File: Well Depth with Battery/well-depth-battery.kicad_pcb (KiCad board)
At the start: 2 copper layers, 28 x 26 mm, 59 parts, among them J1 Conn_01x02_Female, J2 Conn_01x04_Female, J3 Conn_01x04_Male, J4 Conn_01x02_Male, J5 USB_A, Q1 Q_NMOS_GSD, Q2 Q_PMOS_GSD, Q3 Q_PMOS_GSD, U1 LM358, U2 LM358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

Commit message: WDB: Floorplanning
Also fixed .gitignore to not ignore lib
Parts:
- removed H4: MountingHole, MountingHole:MountingHole_3.2mm_M3
- J5: footprint Connector_USB:USB_A_Molex_67643_Horizontal -> Connector_USB:USB_A_Molex_105057_Vertical
- moved J5 91.1 mm to (83.5, 116.4)
- moved U6 76.1 mm to (89.2, 104.6), turned to -90 degrees
- moved R21 76.0 mm to (107.0, 105.8), turned to 90 degrees
- moved R20 76.0 mm to (105.8, 110.8), turned to 180 degrees
- moved H1 75.5 mm to (74.8, 114.5)
- moved H3 75.2 mm to (99.2, 115.2)
- moved C14 74.5 mm to (90.7, 99.6)
- moved R6 71.6 mm to (105.4, 103.0), turned to 90 degrees
- moved Y1 68.2 mm to (88.6, 97.2), turned to 180 degrees
- moved R16 67.9 mm to (94.0, 101.0), turned to -90 degrees
- moved C11 65.6 mm to (86.6, 96.7), turned to 90 degrees
- moved C12 63.4 mm to (90.6, 97.2), turned to 90 degrees
- moved C3 62.1 mm to (94.8, 107.5), turned to 90 degrees
- moved R7 60.9 mm to (96.2, 107.5), turned to -90 degrees
- moved D3 60.4 mm to (103.5, 86.0)
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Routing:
- net GND: track 83.3 -> 0.00 mm, vias 3 -> 0
- net VDD: track 43.7 -> 0.00 mm, vias 2 -> 0
- net Net-(Q1-Pad3): track 19.0 -> 0.00 mm, vias 2 -> 0
- net Net-(C4-Pad1): track 18.0 -> 0.00 mm, vias 1 -> 0
- net /A_ON: track 17.2 -> 0.00 mm, vias 1 -> 0
- net Net-(C3-Pad1): track 16.4 -> 0.00 mm
- net +9V: track 11.5 -> 0.00 mm
- net Net-(C4-Pad2): track 7.73 -> 0.00 mm
- net Net-(C5-Pad2): track 7.39 -> 0.00 mm
- net Net-(C10-Pad2): track 7.15 -> 0.00 mm
- net Net-(C1-Pad2): track 7.14 -> 0.00 mm
- net Net-(C8-Pad2): track 7.13 -> 0.00 mm
- net Net-(C3-Pad2): track 7.10 -> 0.00 mm
- net Net-(C8-Pad1): track 5.83 -> 0.00 mm
- net Net-(R12-Pad2): track 4.75 -> 0.00 mm
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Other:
- board size 28 x 26 mm -> 45.4 x 48.3 mm
- board text removed: "+"
- board text removed: "+9V"
- board text removed: "-"
- board text removed: "EWB-SFP"
- board text removed: "GAIN"
- board text removed: "GND"
- board text removed: "OFFSET"
- board text removed: "ON"
- board text removed: "SIG"
- board text removed: "Well Depth Frontend"

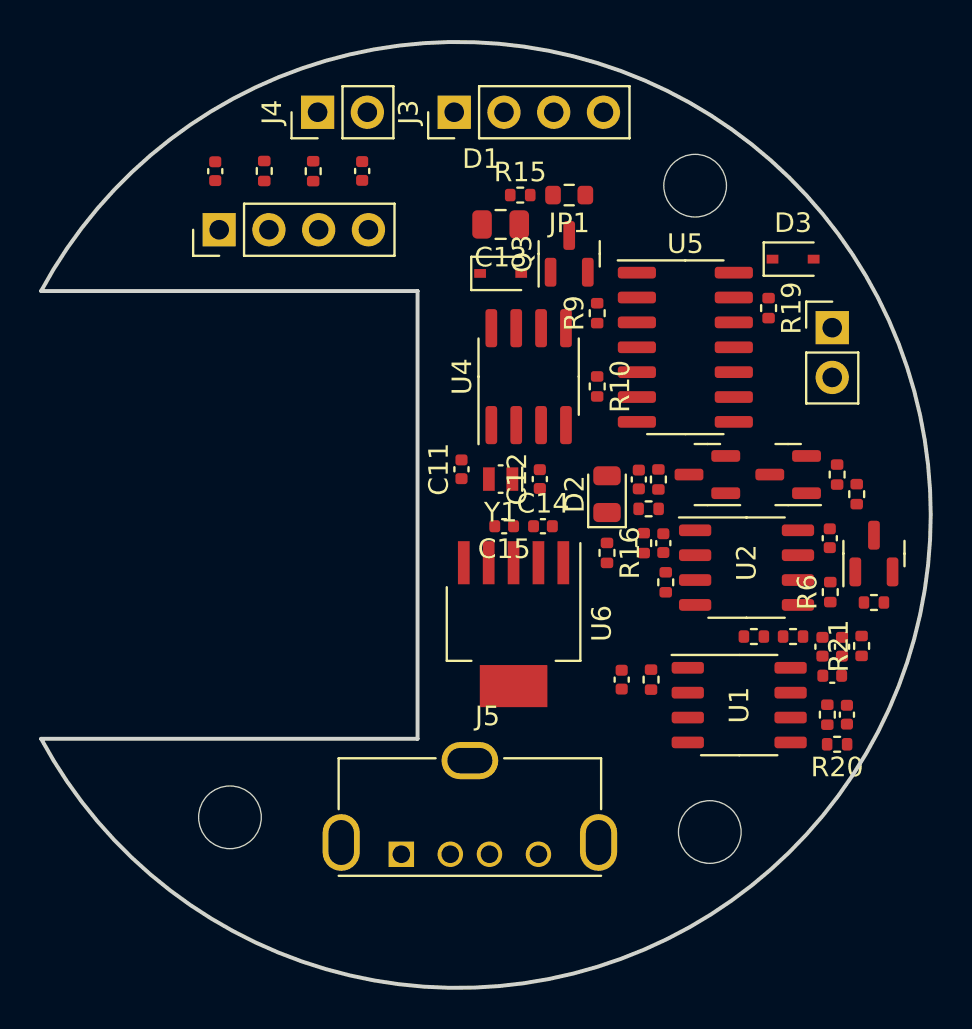
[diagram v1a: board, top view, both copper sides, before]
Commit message: WDB: New Board Outline
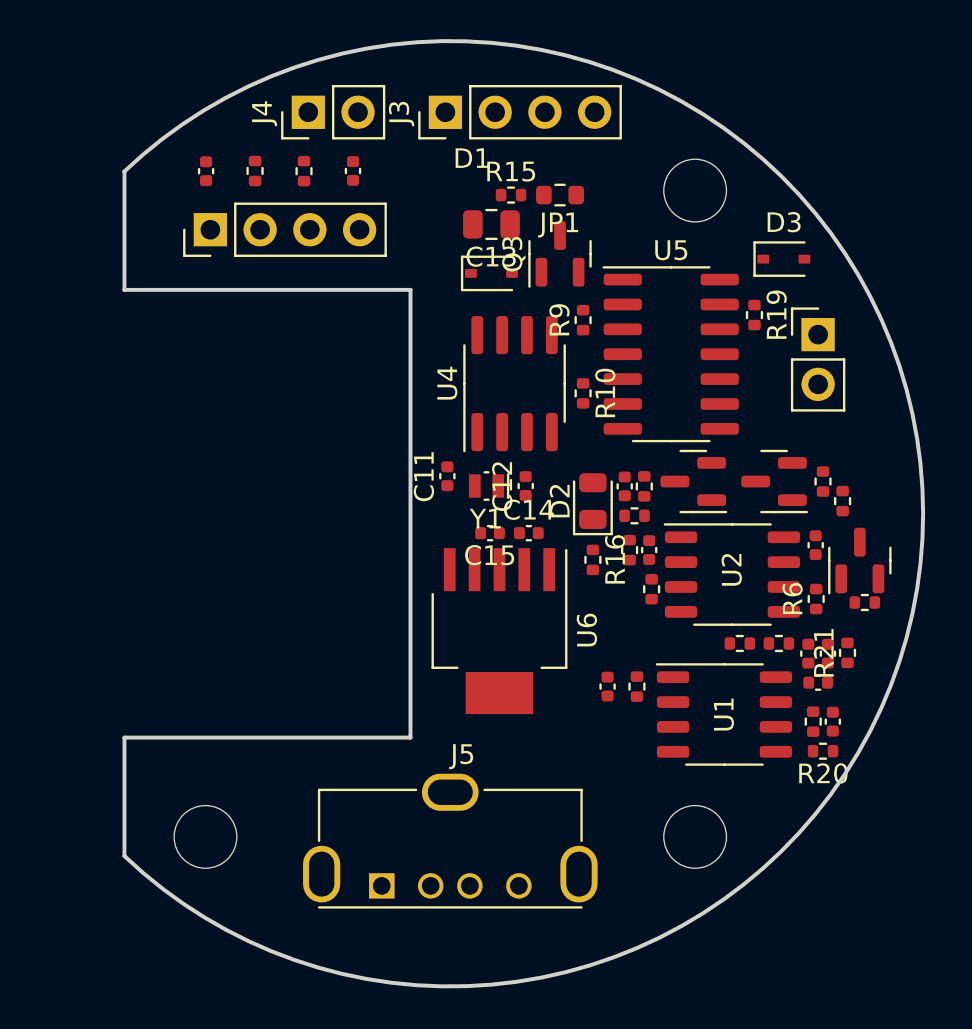
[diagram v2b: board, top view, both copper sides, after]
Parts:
- moved J5 1.90 mm to (82.5, 118.0)
- moved H1 1.60 mm to (73.5, 115.5)
- moved U1 0.89 mm to (100.0, 109.2)
- moved C10 0.80 mm to (94.9, 97.6)
- moved C14 0.80 mm to (90.0, 100.0)
- moved C15 0.80 mm to (88.0, 100.0)
- moved C3 0.80 mm to (94.0, 107.8)
- moved C6 0.80 mm to (104.8, 107.6)
- moved C8 0.80 mm to (96.2, 100.9)
- moved C9 0.80 mm to (104.7, 100.6)
- moved D2 0.80 mm to (93.3, 98.4)
- moved J1 0.80 mm to (104.8, 89.9)
- moved Q1 0.80 mm to (106.9, 101.4)
- moved Q2 0.80 mm to (102.5, 97.4)
- moved R1 0.80 mm to (105.0, 97.4)
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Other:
- board size 45.4 x 48.3 mm -> 40.8 x 48.3 mm

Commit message: WDB: Layout and CAM
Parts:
- moved C11 0.92 mm to (85.8, 98.0), turned to -90 degrees
- moved R2 0.47 mm to (107.2, 104.0)
- moved C9 0.36 mm to (104.7, 100.2), turned to -90 degrees
- moved R11 0.18 mm to (96.1, 102.9)
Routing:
- net GND: track 0.00 -> 181.7 mm, vias 0 -> 7
- net VDD: track 0.00 -> 57.1 mm, vias 0 -> 2
- net +3V3: track 0.00 -> 52.8 mm, vias 0 -> 2
- net Net-(C1-Pad2): track 0.00 -> 49.6 mm, vias 0 -> 2
- net Net-(C2-Pad2): track 0.00 -> 46.8 mm, vias 0 -> 2
- net /USB_D+: track 0.00 -> 46.0 mm, vias 0 -> 1
- net /USB_D-: track 0.00 -> 46.0 mm, vias 0 -> 1
- net +9V: track 0.00 -> 30.6 mm, vias 0 -> 2
- net /SWDIO: track 0.00 -> 27.5 mm, vias 0 -> 1
- net /A_ON: track 0.00 -> 26.1 mm, vias 0 -> 2
- net /SWCLK: track 0.00 -> 23.4 mm, vias 0 -> 1
- net /TXD: track 0.00 -> 22.0 mm, vias 0 -> 1
- net /RXD: track 0.00 -> 20.7 mm, vias 0 -> 1
- net Net-(C3-Pad1): track 0.00 -> 17.0 mm
- net Net-(D2-Pad2): track 0.00 -> 14.3 mm, vias 0 -> 2
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- added copper zone on B.Cu, net GND
- added copper zone on F.Cu, net GND
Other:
- board text added: "+"
- board text added: "+9V"
- board text added: "-"
- board text added: "3V3"
- board text added: "GND"
- board text added: "RX"
- board text added: "SWCLK"
- board text added: "SWDIO"
- board text added: "TX"
- board text added: "Well Monitor EWB-SFP Hans Gaensbauer & Riley Lymann"

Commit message: WDB: DRC Pass and Fab
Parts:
- removed D1: D_Schottky_Small, Diode_SMD:D_SOD-323
- removed JP1: SolderJumper_2_Open, Resistor_SMD:R_0603_1608Metric
- removed R10, R9: 10k, Resistor_SMD:R_0402_1005Metric
- removed R15: 100k, Resistor_SMD:R_0402_1005Metric
- added C16: 10u, Capacitor_SMD:C_0805_2012Metric, F.Cu at (89.2, 97.8)
- added C17: 1u, Capacitor_SMD:C_0402_1005Metric, F.Cu at (98.2, 87.8)
- added C18: 100n, Capacitor_SMD:C_0402_1005Metric, F.Cu at (96.2, 95.1)
- added C19: 100n, Capacitor_SMD:C_0402_1005Metric, F.Cu at (97.2, 86.8)
- added FB1: FerriteBead_Small, Resistor_SMD:R_0402_1005Metric, F.Cu at (94.2, 94.8)
- added J6: Conn_02x05_Odd_Even, EWB:3221-10-0300-00-TR, B.Cu at (92.5, 91.5)
- added TP1: TestPoint, TestPoint:TestPoint_THTPad_1.5x1.5mm_Drill0.7mm, F.Cu at (104.2, 86.5)
- J3: value Conn_01x04_Male -> Micro_SD_Card; footprint Connector_PinHeader_2.54mm:PinHeader_1x04_P2.54mm_Vertical -> EWB:MEM2051-00-195-00-A; moved to B.Cu
- Q3: moved to B.Cu
- R16: value 200 -> 470
- U4: value PCF85263AT -> NCP1117-5.0_SOT223; footprint Package_SO:SOIC-8_3.9x4.9mm_P1.27mm -> Package_TO_SOT_SMD:SOT-223-3_TabPin2
- U5: value ATSAMD11C14A-SS -> ATSAMD21E17D-M; footprint Package_SO:SOIC-14_3.9x8.7mm_P1.27mm -> Package_DFN_QFN:QFN-32-1EP_5x5mm_P0.5mm_EP3.6x3.6mm
- moved J3 26.9 mm to (95.8, 103.5), turned to -90 degrees
- moved R16 14.7 mm to (107.5, 97.5)
- moved C13 13.9 mm to (91.5, 97.8), turned to 90 degrees
- moved D2 13.6 mm to (106.5, 95.2), turned to 180 degrees
- moved Q3 13.5 mm to (85.8, 97.9), turned to -90 degrees
- moved C11 12.2 mm to (93.8, 88.8), turned to 0 degrees
- moved R19 11.1 mm to (93.8, 96.8)
- moved Y1 9.06 mm to (93.5, 90.5), turned to 90 degrees
- moved J4 7.49 mm to (86.2, 78.0)
- moved D3 6.75 mm to (103.2, 92.8), turned to -90 degrees
- moved C12 6.46 mm to (93.5, 92.2), turned to 180 degrees
- moved U4 1.56 mm to (88.5, 91.0)
- moved J1 1.47 mm to (106.2, 89.9)
- moved U5 0.97 mm to (98.0, 91.5)
- moved R11 0.74 mm to (96.1, 103.6)
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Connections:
- C13 pad 1: Net-(C13-Pad1) -> GND
- C13 pad 2: GND -> VDD
- J3 pad 1: +3V3 -> unconnected-(J3-Pad1)
- J3 pad 2: /SWCLK -> /~{CS}
- J3 pad 3: /SWDIO -> /SDO
- J3 pad 4: GND -> Net-(J3-Pad4)
- J5 pad 1: unconnected-(J5-Pad1) -> Net-(C16-Pad2)
- Q3 pad 1: Net-(C13-Pad1) -> /SD_POW_~{EN}
- Q3 pad 3: Net-(Q3-Pad3) -> Net-(J3-Pad4)
- U4 pad 1: Net-(C11-Pad1) -> GND
- U4 pad 2: Net-(C12-Pad1) -> Net-(C16-Pad2)
- U4 pad 3: +3V3 -> VDD
- U5 pad 1: /A_ON -> Net-(C11-Pad1)
- U5 pad 10: /USB_D+ -> GND
- U5 pad 11: GND -> /SD_POW_~{EN}
- U5 pad 12: Net-(Q3-Pad3) -> /A_ON
- U5 pad 13: /VOUT -> /TXD
- U5 pad 14: Net-(D2-Pad2) -> /RXD
- U5 pad 2: /TXD -> Net-(C12-Pad1)
- U5 pad 3: /RXD -> /VOUT
- U5 pad 4: /SDA -> unconnected-(U5-Pad4)
- U5 pad 5: /SCL -> unconnected-(U5-Pad5)
- U5 pad 7: /SWCLK -> unconnected-(U5-Pad7)
- U5 pad 8: /SWDIO -> unconnected-(U5-Pad8)
- U5 pad 9: /USB_D- -> Net-(C18-Pad2)
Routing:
- net GND: track 181.7 -> 92.1 mm, vias 7 -> 8
- net Net-(C16-Pad2): track 0.00 -> 37.5 mm, vias 0 -> 1
- net /VOUT: track 4.32 -> 27.5 mm, vias 0 -> 2
- net /SD_POW_~{EN}: track 0.00 -> 18.7 mm, vias 0 -> 1
- net /~{CS}: track 0.00 -> 17.2 mm, vias 0 -> 1
- net Net-(J3-Pad4): track 0.00 -> 16.3 mm
- net +3V3: track 52.8 -> 37.1 mm, vias 2 -> 3
- net /SWDIO: track 27.5 -> 12.2 mm
- net /~{SRST}: track 0.00 -> 14.9 mm, vias 0 -> 1
- net /SDO: track 0.00 -> 14.1 mm, vias 0 -> 1
- net /SCK: track 0.00 -> 11.7 mm, vias 0 -> 1
- net /SDI: track 0.00 -> 11.2 mm, vias 0 -> 1
- net /SWCLK: track 23.4 -> 12.6 mm
- net Net-(C10-Pad2): track 12.3 -> 2.16 mm, vias 2 -> 0
- net Net-(Q3-Pad3): track 10.1 -> 0.00 mm
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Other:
- board text removed: "3V3"
- board text removed: "SWCLK"
- board text removed: "SWDIO"
- board text removed: "Well Monitor EWB-SFP Hans Gaensbauer & Riley Lymann"

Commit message: First pass routing for rectangular board
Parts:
- removed J5: USB_A, Connector_USB:USB_A_Molex_105057_Vertical
- removed Q3: Q_PMOS_GSD, Package_TO_SOT_SMD:SOT-23
- added H4: MountingHole, MountingHole:MountingHole_3.2mm_M3, F.Cu at (143.0, 137.0)
- added R10: 100k, Resistor_SMD:R_0402_1005Metric, F.Cu at (149.5, 123.1)
- added R9: 100k, Resistor_SMD:R_0402_1005Metric, F.Cu at (147.5, 123.1)
- added RV1: 100k, Potentiometer_SMD:Potentiometer_Bourns_3314J_Vertical, F.Cu at (162.8, 118.0)
- added RV2: 1k, Potentiometer_SMD:Potentiometer_Bourns_3314J_Vertical, F.Cu at (163.0, 128.0)
- J3: value Micro_SD_Card -> Conn_02x04_Odd_Even; footprint EWB:MEM2051-00-195-00-A -> EWB:CardEdge_Prog; moved to F.Cu
- J6: value Conn_02x05_Odd_Even -> Conn_01x04; footprint EWB:3221-10-0300-00-TR -> Connector_PinHeader_2.54mm:PinHeader_2x02_P2.54mm_Vertical; moved to F.Cu
- moved C1 82.2 mm to (142.0, 127.0)
- moved C2 82.2 mm to (149.5, 127.0)
- moved R4 82.2 mm to (144.5, 127.0)
- moved R5 82.2 mm to (147.0, 127.0)
- moved J2 82.2 mm to (142.2, 130.0)
- moved H1 76.7 mm to (143.0, 83.0)
- moved C13 75.3 mm to (166.8, 99.6)
- moved C15 75.3 mm to (163.3, 101.8)
- moved C16 75.3 mm to (164.6, 99.6)
- moved U4 75.3 mm to (163.8, 92.8)
- moved C14 75.3 mm to (165.3, 101.8)
- moved U6 75.3 mm to (163.8, 106.8)
- moved H3 71.8 mm to (167.0, 137.0)
- moved J3 70.9 mm to (157.4, 138.5), turned to 180 degrees
- moved H2 68.5 mm to (167.0, 83.0)
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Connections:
- C16 pad 2: Net-(C16-Pad2) -> Net-(J6-Pin_4)
- J3 pad 1: unconnected-(J3-Pad1) -> +3V3
- J3 pad 2: /~{CS} -> /SWDIO
- J3 pad 3: /SDO -> GND
- J3 pad 4: Net-(J3-Pad4) -> /SWCLK
- J3 pad 5: /SCK -> GND
- J3 pad 6: GND -> unconnected-(J3-Pin_6-Pad6)
- J3 pad 7: /SDI -> GND
- J3 pad 8: unconnected-(J3-Pad8) -> /~{SRST}
- J6 pad 1: +3V3 -> GND
- J6 pad 2: /SWDIO -> /USB_D-
- J6 pad 3: GND -> /USB_D+
- J6 pad 4: /SWCLK -> Net-(J6-Pin_4)
- U4 pad 2: Net-(C16-Pad2) -> Net-(J6-Pin_4)
- U5 pad 11: /SD_POW_~{EN} -> unconnected-(U5-PA08-Pad11)
- U5 pad 17: /SDO -> unconnected-(U5-PA16-Pad17)
- U5 pad 18: /SCK -> unconnected-(U5-PA17-Pad18)
- U5 pad 19: /~{CS} -> unconnected-(U5-PA18-Pad19)
- U5 pad 20: /SDI -> unconnected-(U5-PA19-Pad20)
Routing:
- net VDD: track 58.4 -> 119.6 mm, vias 4 -> 5
- net Net-(U1B-+): track 54.7 -> 9.95 mm, vias 2 -> 0
- net Net-(U1A-+): track 55.9 -> 11.3 mm, vias 2 -> 0
- net +3V3: track 37.1 -> 79.0 mm, vias 3 -> 4
- net /SWDIO: track 12.2 -> 54.0 mm, vias 1 -> 2
- net /SWCLK: track 12.6 -> 53.0 mm, vias 1 -> 2
- net /USB_D+: track 48.9 -> 10.9 mm
- net Net-(C16-Pad2): track 37.5 -> 0.00 mm, vias 1 -> 0
- net /~{SRST}: track 14.9 -> 52.2 mm
- net /USB_D-: track 49.3 -> 15.3 mm
- net GND: track 92.1 -> 65.5 mm, vias 8 -> 2
- net /SD_POW_~{EN}: track 18.7 -> 0.00 mm, vias 1 -> 0
- net Net-(J6-Pin_4): track 0.00 -> 17.8 mm
- net /~{CS}: track 17.2 -> 0.00 mm, vias 1 -> 0
- net Net-(J3-Pad4): track 16.3 -> 0.00 mm
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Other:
- board size 40.8 x 48.3 mm -> 30 x 60 mm
- board text removed: "+"
- board text removed: "+9V"
- board text removed: "-"
- board text removed: "GND"
- board text removed: "RX"
- board text removed: "TX"

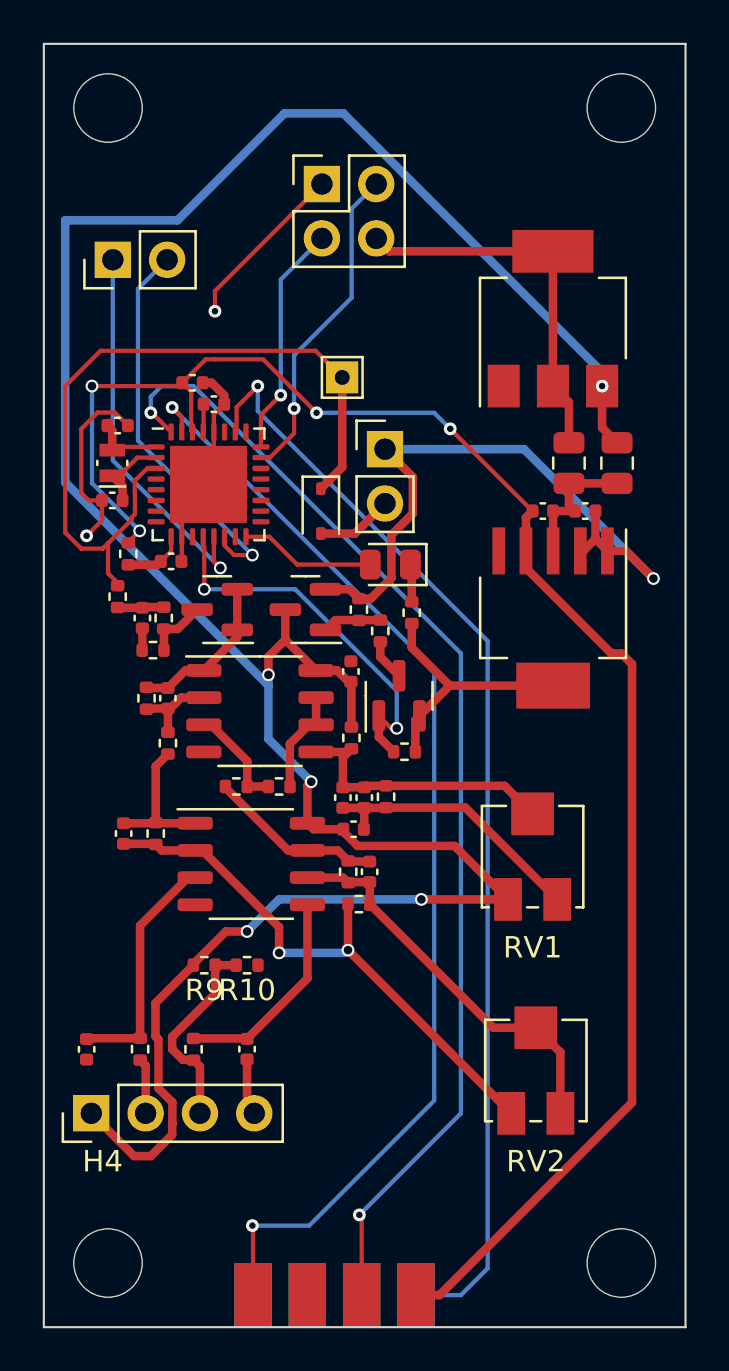
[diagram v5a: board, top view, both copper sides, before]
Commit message: redo routing, DRC/ERC pass
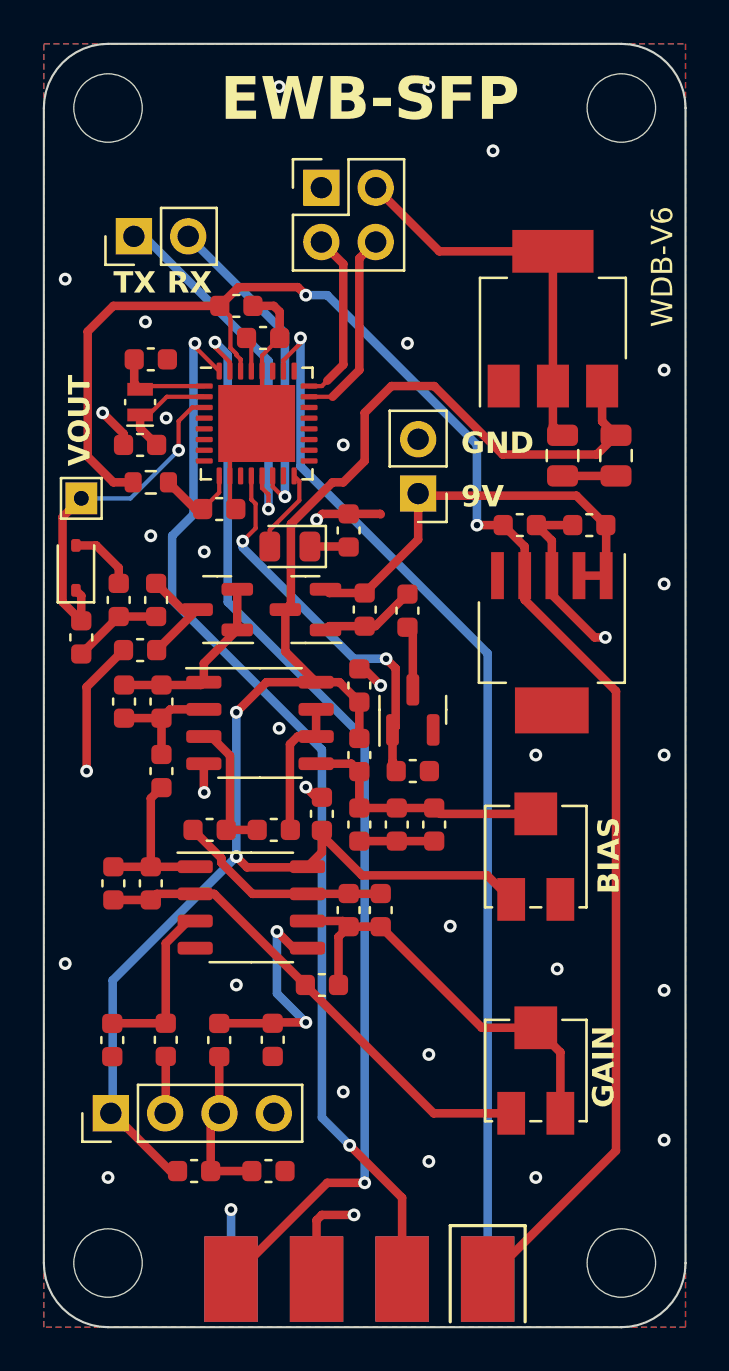
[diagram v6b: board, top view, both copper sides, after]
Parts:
- removed J4: Conn_01x02_Male, Connector_PinHeader_2.54mm:PinHeader_1x02_P2.54mm_Vertical
- added J5: Conn_01x04, Connector_PinHeader_2.54mm:PinHeader_1x04_P2.54mm_Vertical, F.Cu at (143.1, 130.0)
- C1, C10, C11, C12, C14, C15, C17, C18, C19, C2, C3, C4, C5, C6, C7, C8, C9: footprint Capacitor_SMD:C_0402_1005Metric -> Capacitor_SMD:C_0603_1608Metric
- FB1: footprint Resistor_SMD:R_0402_1005Metric -> Resistor_SMD:R_0603_1608Metric
- J1: value Conn_01x02_Female -> Conn_01x02
- J2: value Conn_01x04_Female -> Conn_01x02; footprint Connector_PinHeader_2.54mm:PinHeader_1x04_P2.54mm_Vertical -> Connector_PinHeader_2.54mm:PinHeader_1x02_P2.54mm_Vertical
- R1, R10, R11, R12, R13, R14, R16, R17, R18, R19, R2, R20, R21, R3, R4, R5, R6, R7, R8, R9: footprint Resistor_SMD:R_0402_1005Metric -> Capacitor_SMD:C_0603_1608Metric
- moved J2 41.0 mm to (144.2, 89.0)
- moved TP1 13.4 mm to (141.8, 101.2)
- moved D3 11.8 mm to (141.5, 104.5), turned to 90 degrees
- moved R10 9.68 mm to (150.5, 132.7)
- moved R9 9.64 mm to (147.0, 132.7)
- moved R16 4.85 mm to (154.2, 102.8), turned to 90 degrees
- moved D2 4.78 mm to (151.5, 103.5)
- moved R20 4.16 mm to (153.0, 124.0)
- moved C19 4.14 mm to (149.0, 92.2)
- moved C17 3.86 mm to (150.2, 93.8)
- moved U5 3.63 mm to (149.9, 97.8)
- moved FB1 3.51 mm to (145.0, 100.5), turned to 180 degrees
- moved C11 3.46 mm to (145.0, 94.8)
- moved J3 3.43 mm to (160.8, 137.8)
- moved C18 3.32 mm to (148.2, 101.8)
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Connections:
- net +3V3 renamed +3.3V
- C16 pad 2: Net-(J6-Pin_4) -> Net-(J6-Pin_2)
- J2 pad 1: VDD -> /TXD
- J2 pad 2: Net-(J2-Pin_2) -> /RXD
- J6 pad 2: /USB_D- -> Net-(J6-Pin_2)
- J6 pad 4: Net-(J6-Pin_4) -> /USB_D-
- R10 pad 2: Net-(J2-Pin_3) -> Net-(J5-Pin_3)
- R4 pad 1: Net-(J2-Pin_2) -> Net-(J5-Pin_2)
- R5 pad 1: Net-(J2-Pin_3) -> Net-(J5-Pin_3)
- R9 pad 1: Net-(J2-Pin_3) -> Net-(J5-Pin_3)
- U4 pad 2: Net-(J6-Pin_4) -> Net-(J6-Pin_2)
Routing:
- net VDD: track 119.6 -> 81.1 mm, vias 5 -> 2
- net /VOUT: track 35.9 -> 16.3 mm, vias 0 -> 1
- net Net-(J6-Pin_2): track 0.00 -> 18.3 mm
- net Net-(J6-Pin_4): track 17.8 -> 0.00 mm
- net GND: track 65.5 -> 52.3 mm, vias 2 -> 35
- net +9V: track 31.4 -> 20.6 mm, vias 1 -> 0
- net Net-(J2-Pin_3): track 9.56 -> 0.00 mm
- net Net-(J5-Pin_3): track 0.00 -> 7.52 mm
- net /USB_D-: track 15.3 -> 9.17 mm, vias 1 -> 0
- net /SWDIO: track 54.0 -> 50.4 mm
- net Net-(U1A--): track 26.3 -> 23.0 mm, vias 2 -> 0
- net Net-(U1A-+): track 11.3 -> 8.05 mm
- net /RXD: track 18.5 -> 15.3 mm
- net /USB_D+: track 10.9 -> 8.17 mm, vias 1 -> 0
- net Net-(J5-Pin_2): track 0.00 -> 2.68 mm
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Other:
- outline, holes or cut-outs redrawn
- board text added: "9V"
- board text added: "BIAS"
- board text added: "EWB-SFP"
- board text added: "GAIN"
- board text added: "GND"
- board text added: "RX"
- board text added: "TX"
- board text added: "VOUT"
- board text added: "WDB-V6"
